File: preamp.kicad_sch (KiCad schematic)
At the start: 18 parts, among them U1601 THS4551

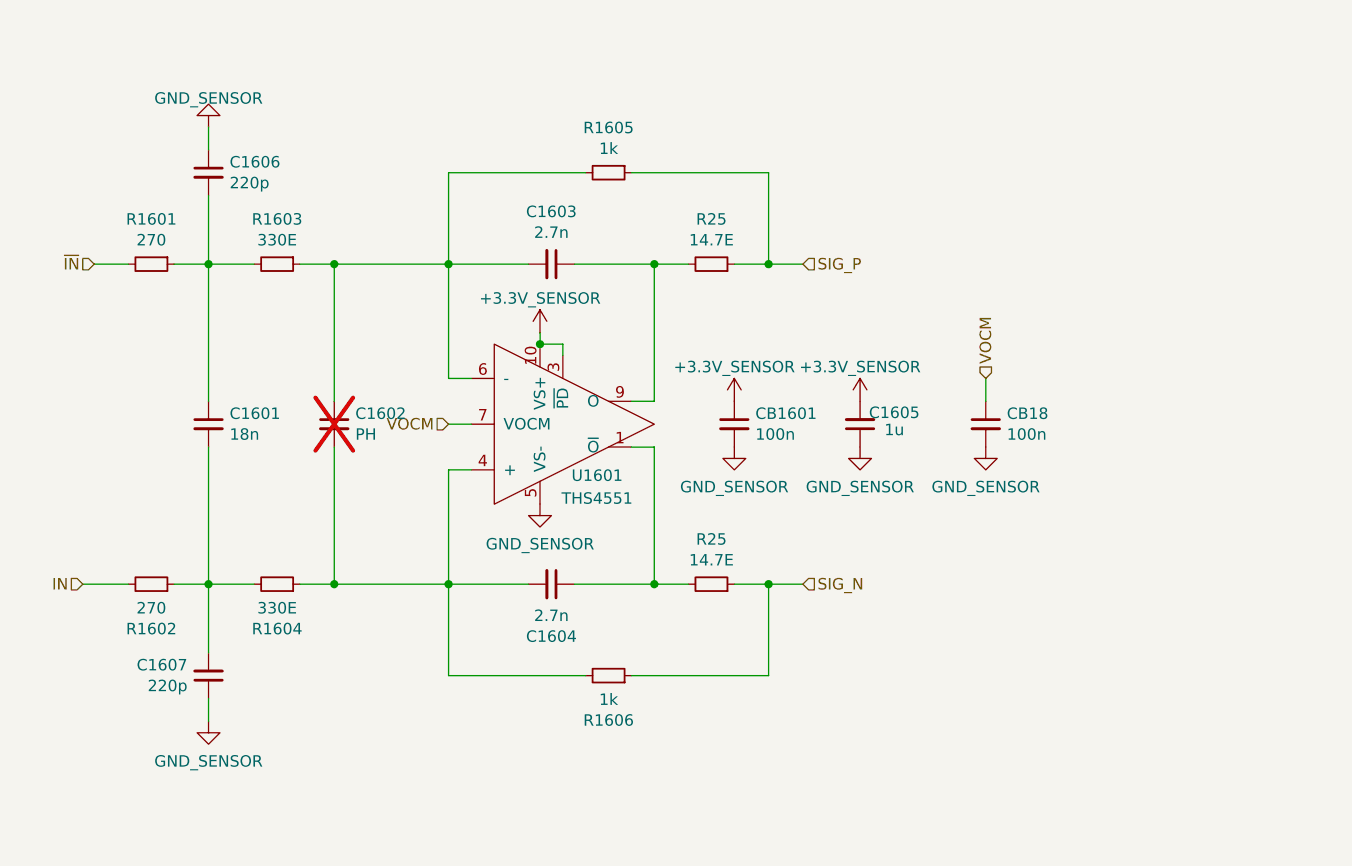
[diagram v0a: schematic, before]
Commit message: (sch) change THS4551 from RUN to RGT
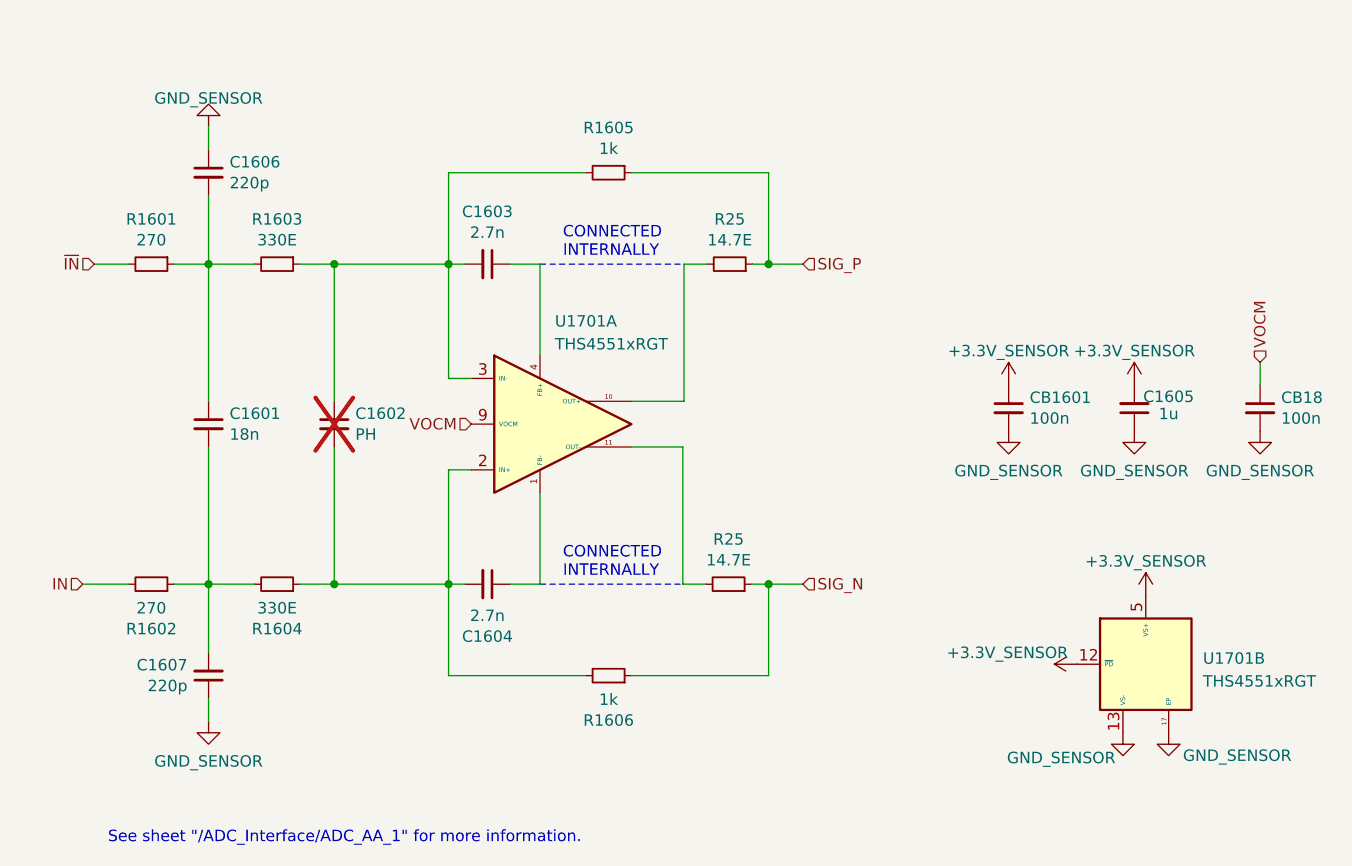
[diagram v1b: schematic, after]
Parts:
- removed U1601: THS4551, grootvoet:WQFN-10_RUN, symbol grootvoet:THS4551
- added U1701: THS4551xRGT, Package_DFN_QFN:VQFN-16-1EP_3x3mm_P0.5mm_EP1.68x1.68mm, symbol grootvoet:THS4551xRGT
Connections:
- net +3.3V: now also U1701.12 (~{PD}), U1701.5 (VS+), U1701.6 (VS+), U1701.7 (VS+), U1701.8 (VS+)
- net GND: now also U1701.13 (VS-), U1701.14 (VS-), U1701.15 (VS-), U1701.16 (VS-), U1701.17 (EP)
- net VOCM: now also U1701.9 (VOCM)
- net at C1604.1: now also U1701.1 (FB-); no longer R25.2
- net at C1602.2, C1604.2, R1604.1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: now also U1701.2 (IN+)
- net at C1602.1, C1603.2, R1603.1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: now also U1701.3 (IN-)
- net at C1603.1: now also U1701.4 (FB+); no longer R25.2
- new net: R25.2, U1701.10 (OUT+)
- new net: R25.2, U1701.11 (OUT-)
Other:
- note added: "CONNECTED INTERNALLY"
- note added: "See sheet "/ADC_Interface/ADC_AA_1" for more information."
- moved on the sheet: C1603, C1604, C1605, CB1601, CB18, R25

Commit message: (pcb) initial layout with new package
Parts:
- U1701: footprint Package_DFN_QFN:VQFN-16-1EP_3x3mm_P0.5mm_EP1.68x1.68mm -> Package_DFN_QFN:VQFN-16-1EP_3x3mm_P0.5mm_EP1.68x1.68mm_ThermalVias
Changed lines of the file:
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@@
       (effects (font (size 1.27 1.27)) (justify left))
     )
-    (property "Footprint" "Package_DFN_QFN:VQFN-16-1EP_3x3mm_P0.5mm_EP1.68x1.68mm" (at 209.55 124.46 0)
+    (property "Footprint" "Package_DFN_QFN:VQFN-16-1EP_3x3mm_P0.5mm_EP1.68x1.68mm_ThermalVias" (at 209.55 124.46 0)
       (effects (font (size 1.27 1.27)) hide)
     )
     (property "Datasheet" "https://www.ti.com/lit/ds/symlink/ths4551.pdf" (at 209.55 124.46 0)
+      (effects (font (size 1.27 1.27)) hide)
+    )
+    (property "MPN" "" (at 209.55 124.46 0)
+      (effects (font (size 1.27 1.27)) hide)
+    )
+    (property "Mfr." "" (at 209.55 124.46 0)
       (effects (font (size 1.27 1.27)) hide)
     )
@@
       (effects (font (size 1.27 1.27)) (justify left))
     )
-    (property "Footprint" "Package_DFN_QFN:VQFN-16-1EP_3x3mm_P0.5mm_EP1.68x1.68mm" (at 144.78 97.79 0)
+    (property "Footprint" "Package_DFN_QFN:VQFN-16-1EP_3x3mm_P0.5mm_EP1.68x1.68mm_ThermalVias" (at 144.78 97.79 0)
       (effects (font (size 1.27 1.27)) hide)
     )
@@
       (effects (font (size 1.27 1.27)) hide)
     )
+    (property "MPN" "" (at 144.78 97.79 0)
+      (effects (font (size 1.27 1.27)) hide)
+    )
+    (property "Mfr." "" (at 144.78 97.79 0)
+      (effects (font (size 1.27 1.27)) hide)
+    )

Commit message: replace passives with 0402
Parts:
- C1605: footprint Capacitor_SMD:C_0603_1608Metric_Pad1.08x0.95mm_HandSolder -> Capacitor_SMD:C_0402_1005Metric; MPN C0603C105K8RACTU -> C0402C105K9PACTU
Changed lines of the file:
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@@
       (effects (font (size 1.27 1.27)))
     )
-    (property "Footprint" "Capacitor_SMD:C_0603_1608Metric_Pad1.08x0.95mm_HandSolder" (at 208.28 96.012 0)
+    (property "Footprint" "Capacitor_SMD:C_0402_1005Metric" (at 208.28 96.012 0)
       (effects (font (size 1.27 1.27)) hide)
     )
@@
       (effects (font (size 1.27 1.27)) hide)
     )
-    (property "MPN" "C0603C105K8RACTU" (at 208.28 96.012 0)
+    (property "MPN" "C0402C105K9PACTU" (at 208.28 96.012 0)
       (effects (font (size 1.27 1.27)) hide)
     )

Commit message: (sch) fix THS4551 3d model
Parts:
- U1701: footprint Package_DFN_QFN:VQFN-16-1EP_3x3mm_P0.5mm_EP1.68x1.68mm_ThermalVias -> grootvoet:VQFN-16-1EP_3x3mm_P0.5mm_EP1.68x1.68mm_ThermalVias
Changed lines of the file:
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@@
       (effects (font (size 1.27 1.27)) (justify left))
     )
-    (property "Footprint" "Package_DFN_QFN:VQFN-16-1EP_3x3mm_P0.5mm_EP1.68x1.68mm_ThermalVias" (at 209.55 124.46 0)
+    (property "Footprint" "grootvoet:VQFN-16-1EP_3x3mm_P0.5mm_EP1.68x1.68mm_ThermalVias" (at 209.55 124.46 0)
       (effects (font (size 1.27 1.27)) hide)
     )
@@
       (effects (font (size 1.27 1.27)) (justify left))
     )
-    (property "Footprint" "Package_DFN_QFN:VQFN-16-1EP_3x3mm_P0.5mm_EP1.68x1.68mm_ThermalVias" (at 144.78 97.79 0)
-      (effects (font (size 1.27 1.27)) hide)
-    )
+    (property "Footprint" "grootvoet:VQFN-16-1EP_3x3mm_P0.5mm_EP1.68x1.68mm_ThermalVias" (at 144.78 97.79 0)
+      (effects (font (size 1.27 1.27)) hide)
+    )

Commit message: (pcb) layout summing out
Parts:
- C1602: footprint Resistor_SMD:R_0603_1608Metric_Pad0.98x0.95mm_HandSolder -> Resistor_SMD:R_0402_1005Metric
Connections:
- net at C1601.1, C1606.2, R1601.1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: now also R1605.2
- net FDA_~{IN}: now reaches C1602.1, C1603.2, R1603.1, U1701.3 (IN-)
- net FDA_~{IN}: no longer R1605.2
- net FB: now reaches C1603.1, U1701.4 (FB+)
- net FDA_IN: now reaches C1602.2, C1604.2, R1604.1, U1701.2 (IN+)
- net FDA_IN: no longer R1606.2
- net at C1601.2, C1607.2, R1602.1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: now also R1606.2
- net ~{FB}: now reaches C1604.1, U1701.1 (FB-)
- net OUT: now reaches R25.2, U1701.10 (OUT+)
- net ~{OUT}: now reaches R25.2, U1701.11 (OUT-)
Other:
- moved on the sheet: C1606, C1607
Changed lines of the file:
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@@
     (comment 4 "License: CERN-OHL-S-2.0")
   )
+  (junction (at 105.41 69.85) (diameter 0) (color 0 0 0 0)
+  )
   (junction (at 105.41 115.57) (diameter 0) (color 0 0 0 0)
   )
@@
   (junction (at 119.38 115.57) (diameter 0) (color 0 0 0 0)
   )
+  (junction (at 105.41 125.73) (diameter 0) (color 0 0 0 0)
+  )
   (junction (at 132.08 80.01) (diameter 0) (color 0 0 0 0)
   )
@@
     (stroke (width 0) (type default))
   )
-  (wire (pts (xy 132.08 125.73) (xy 132.08 115.57))
-    (stroke (width 0) (type default))
-  )
-  (wire (pts (xy 105.41 130.81) (xy 105.41 128.27))
+  (wire (pts (xy 105.41 69.85) (xy 147.32 69.85))
+    (stroke (width 0) (type default))
+  )
+  (wire (pts (xy 105.41 135.255) (xy 105.41 132.715))
     (stroke (width 0) (type default))
   )
@@
     (stroke (width 0) (type default))
   )
+  (wire (pts (xy 105.41 125.73) (xy 105.41 115.57))
+    (stroke (width 0) (type default))
+  )
   (wire (pts (xy 132.08 92.71) (xy 134.62 92.71))
     (stroke (width 0) (type default))
   )
-  (wire (pts (xy 132.08 69.85) (xy 132.08 80.01))
+  (wire (pts (xy 105.41 69.85) (xy 105.41 80.01))
     (stroke (width 0) (type default))
   )
@@
     (stroke (width 0) (type default))
   )
-  (wire (pts (xy 147.32 125.73) (xy 132.08 125.73))
+  (wire (pts (xy 105.41 125.73) (xy 147.32 125.73))
     (stroke (width 0) (type default))
   )
@@
     (stroke (width 0) (type default))
   )
-  (wire (pts (xy 105.41 123.19) (xy 105.41 115.57))
+  (wire (pts (xy 105.41 127.635) (xy 105.41 125.73))
     (stroke (width 0) (type default))
   )
@@
     (stroke (width 0) (type default))
   )
-  (wire (pts (xy 105.41 72.39) (xy 105.41 80.01))
+  (wire (pts (xy 105.41 64.77) (xy 105.41 69.85))
     (stroke (width 0) (type default))
   )
@@
     (stroke (width 0) (type default))
   )
-  (wire (pts (xy 105.41 64.77) (xy 105.41 67.31))
+  (wire (pts (xy 105.41 57.15) (xy 105.41 59.69))
     (stroke (width 0) (type default))
   )
@@
   )
   (wire (pts (xy 165.735 115.57) (xy 167.64 115.57))
-    (stroke (width 0) (type default))
-  )
-  (wire (pts (xy 147.32 69.85) (xy 132.08 69.85))
     (stroke (width 0) (type default))
   )
@@
   (text "CONNECTED\nINTERNALLY" (at 144.78 79.375 0)
     (effects (font (size 1.27 1.27)) (justify left bottom))
+  )
+  (label "OUT" (at 153.67 95.25 0) (fields_autoplaced)
+    (effects (font (size 1.27 1.27)) (justify left bottom))
+  )
+  (label "FDA_IN" (at 130.81 115.57 180) (fields_autoplaced)
+    (effects (font (size 1.27 1.27)) (justify right bottom))
+  )
+  (label "FDA_~{IN}" (at 131.445 80.01 180) (fields_autoplaced)
+    (effects (font (size 1.27 1.27)) (justify right bottom))
+  )
+  (label "~{FB}" (at 142.24 115.57 90) (fields_autoplaced)
+    (effects (font (size 1.27 1.27)) (justify left bottom))
+  )
+  (label "~{OUT}" (at 154.305 100.33 0) (fields_autoplaced)
+    (effects (font (size 1.27 1.27)) (justify left bottom))
+  )
+  (label "FB" (at 142.24 80.01 270) (fields_autoplaced)
+    (effects (font (size 1.27 1.27)) (justify right bottom))
   )
   (hierarchical_label "SIG_P" (shape input) (at 171.45 80.01 0) (fields_autoplaced)
@@
       (effects (font (size 1.27 1.27)) (justify left))
     )
-    (property "Footprint" "Resistor_SMD:R_0603_1608Metric_Pad0.98x0.95mm_HandSolder" (at 119.38 97.79 0)
+    (property "Footprint" "Resistor_SMD:R_0402_1005Metric" (at 119.38 97.79 0)
       (effects (font (size 1.27 1.27)) hide)
     )
     (property "Datasheet" "~" (at 119.38 97.79 0)
+      (effects (font (size 1.27 1.27)) hide)
+    )
+    (property "MPN" "" (at 119.38 97.79 0)
+      (effects (font (size 1.27 1.27)) hide)
+    )
+    (property "Mfr." "" (at 119.38 97.79 0)
       (effects (font (size 1.27 1.27)) hide)
     )
@@
     )
   )
-  (symbol (lib_id "Device:C_Small") (at 105.41 69.85 0) (unit 1)
-    (in_bom yes) (on_board yes) (dnp no)
-    (property "Reference" "C1606" (at 107.7468 68.6816 0)
+  (symbol (lib_id "Device:C_Small") (at 105.41 62.23 0) (unit 1)
+    (in_bom yes) (on_board yes) (dnp no)
+    (property "Reference" "C1606" (at 107.7468 61.0616 0)
       (effects (font (size 1.27 1.27)) (justify left))
     )
-    (property "Value" "220p" (at 107.7468 70.993 0)
+    (property "Value" "220p" (at 107.7468 63.373 0)
       (effects (font (size 1.27 1.27)) (justify left))
     )
-    (property "Footprint" "Capacitor_SMD:C_0402_1005Metric" (at 105.41 69.85 0)
-      (effects (font (size 1.27 1.27)) hide)
-    )
-    (property "Datasheet" "~" (at 105.41 69.85 0)
-      (effects (font (size 1.27 1.27)) hide)
-    )
-    (property "MPN" "GRT1555C1H221FA02D" (at 105.41 69.85 0)
-      (effects (font (size 1.27 1.27)) hide)
-    )
-    (property "Mfr." "Murata" (at 105.41 69.85 0)
+    (property "Footprint" "Capacitor_SMD:C_0402_1005Metric" (at 105.41 62.23 0)
+      (effects (font (size 1.27 1.27)) hide)
+    )
+    (property "Datasheet" "~" (at 105.41 62.23 0)
+      (effects (font (size 1.27 1.27)) hide)
+    )
+    (property "MPN" "GRT1555C1H221FA02D" (at 105.41 62.23 0)
+      (effects (font (size 1.27 1.27)) hide)
+    )
+    (property "Mfr." "Murata" (at 105.41 62.23 0)
       (effects (font (size 1.27 1.27)) hide)
     )
@@
     )
   )
-  (symbol (lib_id "Device:C_Small") (at 105.41 125.73 0) (mirror x) (unit 1)
-    (in_bom yes) (on_board yes) (dnp no)
-    (property "Reference" "C1607" (at 103.0732 124.5616 0)
+  (symbol (lib_id "Device:C_Small") (at 105.41 130.175 0) (mirror x) (unit 1)
+    (in_bom yes) (on_board yes) (dnp no)
+    (property "Reference" "C1607" (at 103.0732 129.0066 0)
       (effects (font (size 1.27 1.27)) (justify right))
     )
-    (property "Value" "220p" (at 103.0732 126.873 0)
+    (property "Value" "220p" (at 103.0732 131.318 0)
       (effects (font (size 1.27 1.27)) (justify right))
     )
-    (property "Footprint" "Capacitor_SMD:C_0402_1005Metric" (at 105.41 125.73 0)
-      (effects (font (size 1.27 1.27)) hide)
-    )
-    (property "Datasheet" "~" (at 105.41 125.73 0)
-      (effects (font (size 1.27 1.27)) hide)
-    )
-    (property "MPN" "GRT1555C1H221FA02D" (at 105.41 125.73 0)
-      (effects (font (size 1.27 1.27)) hide)
-    )
-    (property "Mfr." "Murata" (at 105.41 125.73 0)
+    (property "Footprint" "Capacitor_SMD:C_0402_1005Metric" (at 105.41 130.175 0)
+      (effects (font (size 1.27 1.27)) hide)
+    )
+    (property "Datasheet" "~" (at 105.41 130.175 0)
+      (effects (font (size 1.27 1.27)) hide)
+    )
+    (property "MPN" "GRT1555C1H221FA02D" (at 105.41 130.175 0)
+      (effects (font (size 1.27 1.27)) hide)
+    )
+    (property "Mfr." "Murata" (at 105.41 130.175 0)
       (effects (font (size 1.27 1.27)) hide)
     )
@@
     )
   )
-  (symbol (lib_id "grootvoet:GND_SENSOR") (at 105.41 130.81 0) (unit 1)
+  (symbol (lib_id "grootvoet:GND_SENSOR") (at 105.41 135.255 0) (unit 1)
     (in_bom yes) (on_board yes) (dnp no) (fields_autoplaced)
-    (property "Reference" "#PWR0226" (at 105.41 137.16 0)
-      (effects (font (size 1.27 1.27)) hide)
-    )
-    (property "Value" "GND_SENSOR" (at 105.41 135.255 0)
-      (effects (font (size 1.27 1.27)))
-    )
-    (property "Footprint" "" (at 105.41 130.81 0)
-      (effects (font (size 1.27 1.27)) hide)
-    )
-    (property "Datasheet" "" (at 105.41 130.81 0)
+    (property "Reference" "#PWR0226" (at 105.41 141.605 0)
+      (effects (font (size 1.27 1.27)) hide)
+    )
+    (property "Value" "GND_SENSOR" (at 105.41 139.7 0)
+      (effects (font (size 1.27 1.27)))
+    )
+    (property "Footprint" "" (at 105.41 135.255 0)
+      (effects (font (size 1.27 1.27)) hide)
+    )
+    (property "Datasheet" "" (at 105.41 135.255 0)
       (effects (font (size 1.27 1.27)) hide)
     )
@@
     )
   )
-  (symbol (lib_id "grootvoet:GND_SENSOR") (at 105.41 64.77 180) (unit 1)
+  (symbol (lib_id "grootvoet:GND_SENSOR") (at 105.41 57.15 180) (unit 1)
     (in_bom yes) (on_board yes) (dnp no) (fields_autoplaced)
-    (property "Reference" "#PWR0226" (at 105.41 58.42 0)
-      (effects (font (size 1.27 1.27)) hide)
-    )
-    (property "Value" "GND_SENSOR" (at 105.41 61.595 0)
-      (effects (font (size 1.27 1.27)))
-    )
-    (property "Footprint" "" (at 105.41 64.77 0)
-      (effects (font (size 1.27 1.27)) hide)
-    )
-    (property "Datasheet" "" (at 105.41 64.77 0)
-      (effects (font (size 1.27 1.27)) hide)
-    )
+    (property "Reference" "#PWR0226" (at 105.41 50.8 0)
+      (effects (font (size 1.27 1.27)) hide)
+    )
+    (property "Value" "GND_SENSOR" (at 105.41 53.975 0)
+      (effects (font (size 1.27 1.27)))
+    )
+    (property "Footprint" "" (at 105.41 57.15 0)
+      (effects (font (size 1.27 1.27)) hide)
+    )
+    (property "Datasheet" "" (at 105.41 57.15 0)
+      (effects (font (size 1.27 1.27)) hide)
+    )

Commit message: (sch) fix board seperate net labels
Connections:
- net +3.3V renamed +3.3V_SENSOR
- net GND renamed GND_SENSOR

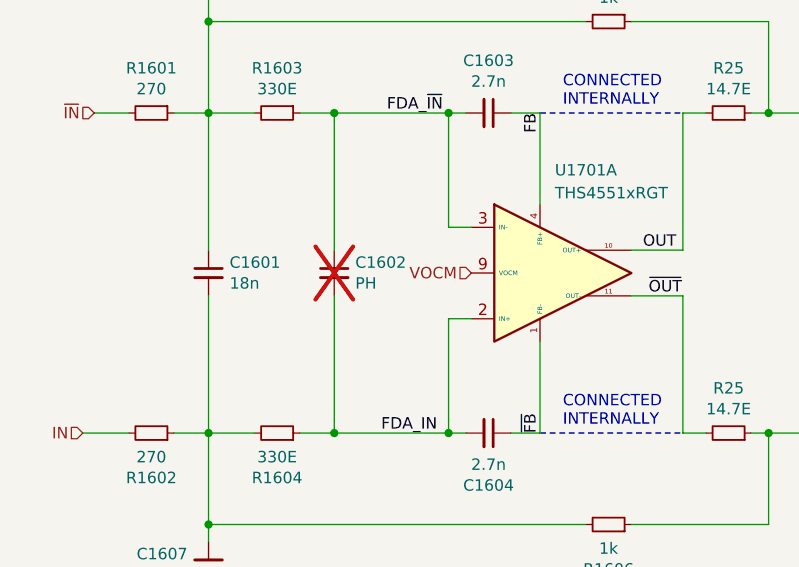
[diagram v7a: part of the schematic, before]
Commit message: (sch) consoldate BOM
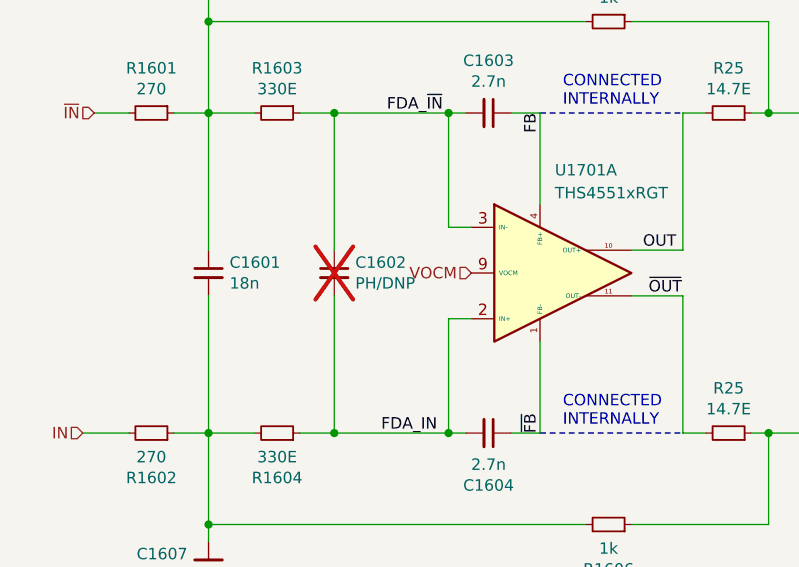
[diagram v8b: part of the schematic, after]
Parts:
- C1602: value PH -> PH/DNP
- U1701: MPN (none) -> THS4551IRGTR; Mfr. (none) -> Texas Instruments
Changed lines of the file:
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@@
       (effects (font (size 1.27 1.27)) (justify left))
     )
-    (property "Value" "PH" (at 121.7168 98.933 0)
+    (property "Value" "PH/DNP" (at 121.7168 98.933 0)
       (effects (font (size 1.27 1.27)) (justify left))
     )
@@
       (effects (font (size 1.27 1.27)) hide)
     )
-    (property "MPN" "" (at 209.55 124.46 0)
-      (effects (font (size 1.27 1.27)) hide)
-    )
-    (property "Mfr." "" (at 209.55 124.46 0)
+    (property "MPN" "THS4551IRGTR" (at 209.55 124.46 0)
+      (effects (font (size 1.27 1.27)) hide)
+    )
+    (property "Mfr." "Texas Instruments" (at 209.55 124.46 0)
       (effects (font (size 1.27 1.27)) hide)
     )
@@
       (effects (font (size 1.27 1.27)) hide)
     )
-    (property "MPN" "" (at 144.78 97.79 0)
-      (effects (font (size 1.27 1.27)) hide)
-    )
-    (property "Mfr." "" (at 144.78 97.79 0)
-      (effects (font (size 1.27 1.27)) hide)
-    )
+    (property "MPN" "THS4551IRGTR" (at 144.78 97.79 0)
+      (effects (font (size 1.27 1.27)) hide)
+    )
+    (property "Mfr." "Texas Instruments" (at 144.78 97.79 0)
+      (effects (font (size 1.27 1.27)) hide)
+    )
